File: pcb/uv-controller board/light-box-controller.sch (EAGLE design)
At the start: 33 parts, among them IC1 LDL112D33R, J1 12 VIN, J2 UVLED-OUT, Q1 FQP30N06L, U1 L7805, U2 ESP-WROOM-32

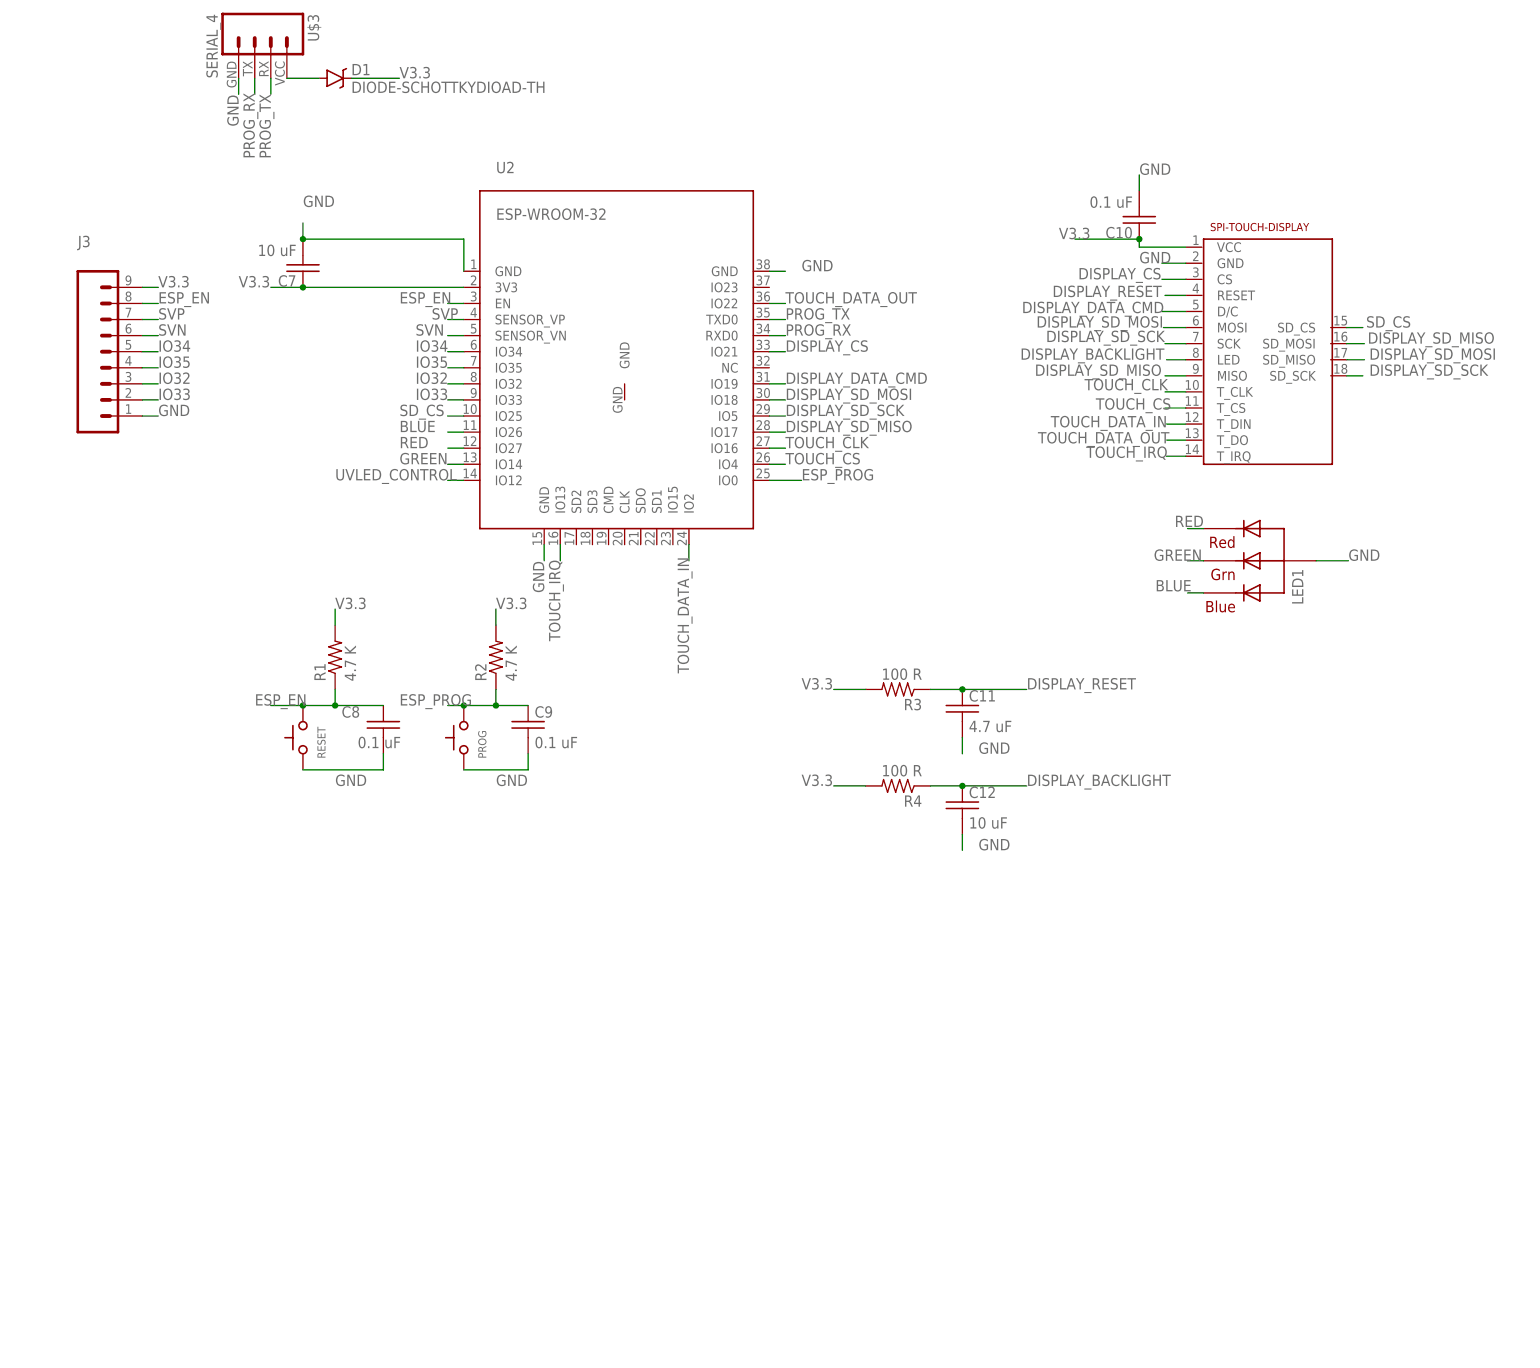
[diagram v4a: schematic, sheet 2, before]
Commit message: adding docs and added voltage multipler for mosfet gate
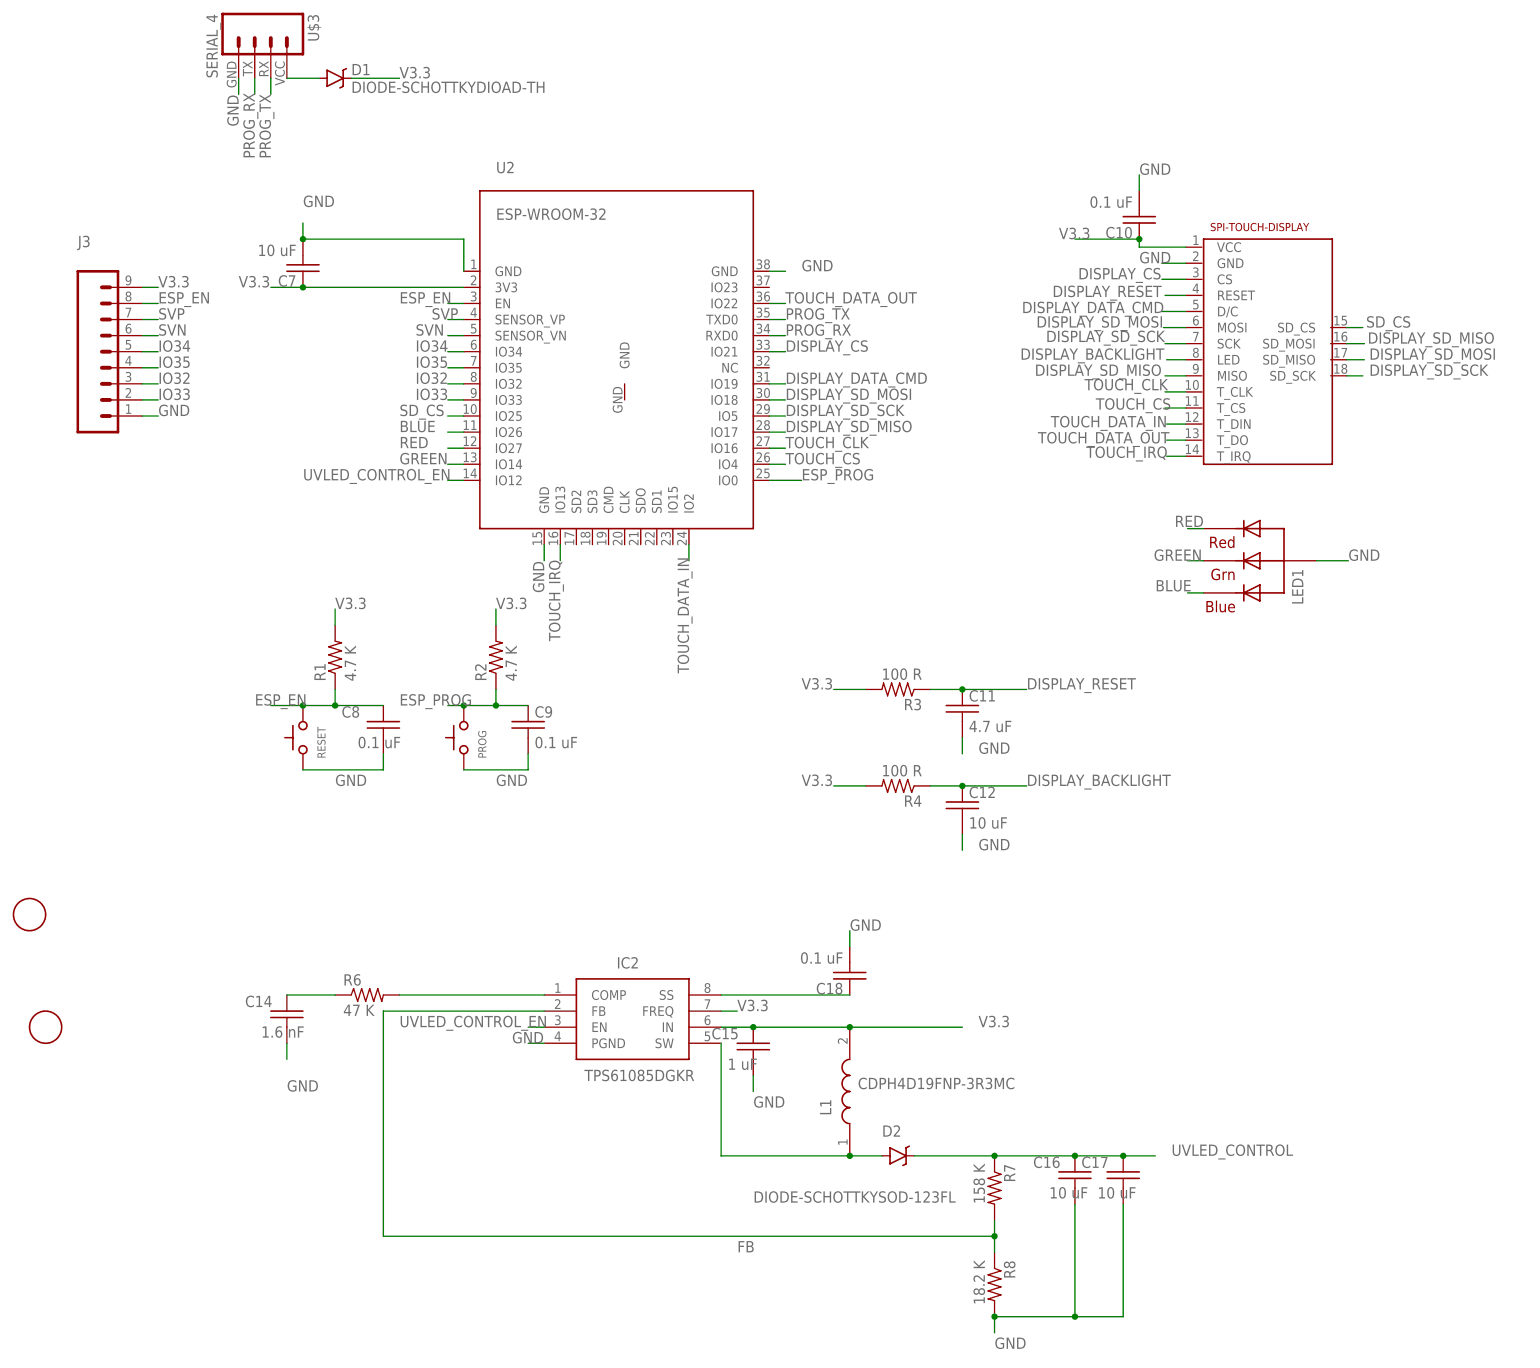
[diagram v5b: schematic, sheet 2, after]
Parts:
- added C14: 1.6 nF, passives:C-USC0805K
- added C15: 1 uF, passives:C-USC0805K
- added C16, C17: 10 uF, passives:C-USC0805K
- added C18: 0.1 uF, passives:C-USC0805K
- added D2: DIODE-SCHOTTKYSOD-123FL, passives:DIODE-SCHOTTKYSOD-123FL
- added IC2: TPS61085DGKR, dc-converters:TPS61085DGKR
- added L1: CDPH4D19FNP-3R3MC, passives:CDPH4D19FNP-3R3MC
- added R6: 47 K, passives:RESISTOR0805-RES
- added R7: 158 K, passives:RESISTOR0805-RES
- added R8: 18.2 K, passives:RESISTOR0805-RES
- added U$5, U$6: FIDUCIAL, logos:FIDUCIAL
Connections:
- new net FB: IC2.FB, R7.2, R8.1
- new net N$3: IC2.COMP, R6.2
- new net N$5: C14.1, R6.1
- new net N$8: C18.1, IC2.SS
- new net UVLED_BEFORE_DIODE: D2.A, IC2.SW, L1.1
- new net UVLED_CONTROL_EN: IC2.EN, U2.IO12
- net GND: now also C14.2, C15.2, C16.2, C17.2, C18.2, IC2.PGND, R8.2
- net UVLED_CONTROL: now also C16.1, C17.1, D2.C, R7.1; no longer U2.IO12
- net V3.3: now also C15.1, IC2.FREQ, IC2.IN, L1.2
